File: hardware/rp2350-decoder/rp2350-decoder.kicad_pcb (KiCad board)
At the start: 6 copper layers, 19.9 x 8.8 mm, 67 parts, among them J1 SWDIO, J2 SWCLK, J3 5052702412, Q1 DMN2991UDA-7B, Q2 DMN2991UDA-7B, Q3 NST847BPDP6T5G, Q4 NST847BPDP6T5G, Q5 DMN2991UDA-7B, Q6 DMN2991UDA-7B, Q7 DMN2991UDA-7B, Q8 DMN2991UDA-7B, SW1 BOOT, U1 NCS2220AMUT1G, U2 AP63203WU, U3 W25Q128JVPIQ, U4 RP2350A, U5 MAX98357AEWL+T, U6 MD9927, Y1 X252012MMB4SI

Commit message: chore: pcb cleanup
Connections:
- net /GPIO21 renamed /DCC_TTL
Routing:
- net GND: track 7.85 -> 6.09 mm
- net +3.3V: track 30.9 -> 29.6 mm
- net /CAP_VDC: track 11.8 -> 10.9 mm
- net /QSPI_CS: track 11.1 -> 10.4 mm

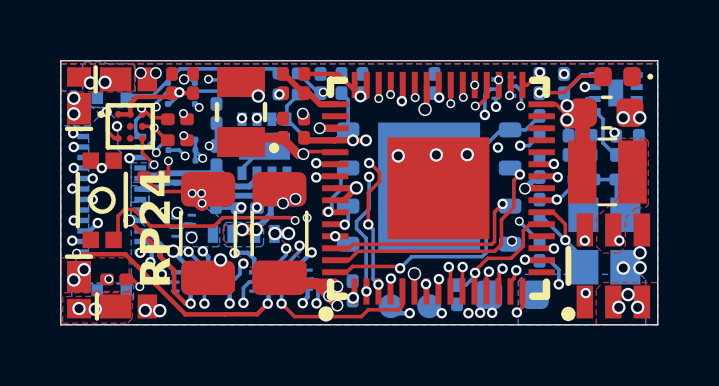
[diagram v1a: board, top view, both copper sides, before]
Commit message: chore: rearrange i2s pins for easier pio use
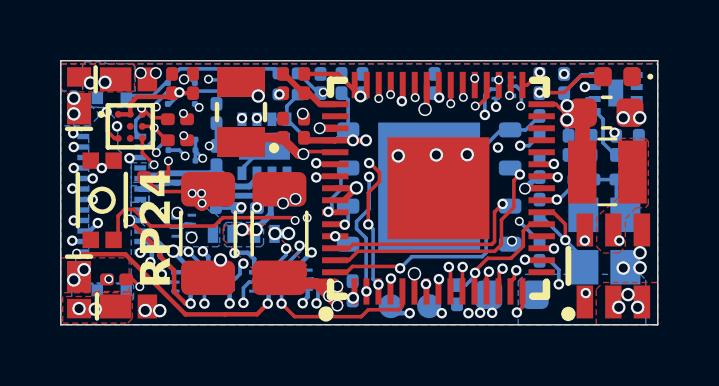
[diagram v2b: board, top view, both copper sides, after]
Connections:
- U4 pad 34: /I2S_LRCLK -> /I2S_DIN
- U4 pad 35: /I2S_DIN -> /I2S_BCLK
- U4 pad 36: /I2S_BCLK -> /I2S_LRCLK
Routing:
- net /I2S_LRCLK: track 17.8 -> 15.8 mm
- net /I2S_BCLK: track 16.0 -> 14.1 mm
- net /I2S_DIN: track 13.1 -> 14.5 mm
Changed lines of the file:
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@@
 			(size 0.88 0.2)
 			(layers "F.Cu" "F.Paste" "F.Mask")
-			(net 39 "/I2S_LRCLK")
+			(net 37 "/I2S_DIN")
 			(pinfunction "GPIO22")
 			(pintype "unspecified")
@@
 			(size 0.88 0.2)
 			(layers "F.Cu" "F.Paste" "F.Mask")
-			(net 37 "/I2S_DIN")
+			(net 38 "/I2S_BCLK")
 			(pinfunction "GPIO23")
 			(pintype "unspecified")
@@
 			(size 0.88 0.2)
 			(layers "F.Cu" "F.Paste" "F.Mask")
-			(net 38 "/I2S_BCLK")
+			(net 39 "/I2S_LRCLK")
 			(pinfunction "GPIO24")
 			(pintype "unspecified")
@@
 		(net 33)
 	)
+	(segment
+		(start 114.2 100.97)
+		(end 114.2 100.56)
+		(width 0.12)
+		(layer "F.Cu")
+		(net 37)
+	)
+	(segment
+		(start 113.817602 101.260002)
+		(end 113.909998 101.260002)
+		(width 0.12)
+		(layer "F.Cu")
+		(net 37)
+	)
+	(segment
+		(start 113.909998 101.260002)
+		(end 114.2 100.97)
+		(width 0.12)
+		(layer "F.Cu")
+		(net 37)
+	)
 	(via
 		(at 101.87707 101.935026)
@@
 	)
 	(via
-		(at 113.8 100.56)
+		(at 113.817602 101.260002)
 		(size 0.3)
 		(drill 0.2)
@@
 	)
 	(segment
-		(start 104.440769 100.946004)
-		(end 104.238673 101.1481)
+		(start 104.796542 100.946004)
+		(end 105.492546 100.25)
 		(width 0.12)
 		(layer "In4.Cu")
@@
 	)
 	(segment
-		(start 101.87707 101.637546)
-		(end 101.87707 101.935026)
+		(start 104.238673 101.1481)
+		(end 104.440769 100.946004)
 		(width 0.12)
 		(layer "In4.Cu")
@@
 	)
 	(segment
-		(start 103.340573 100.97)
-		(end 102.544616 100.97)
+		(start 104.440769 100.946004)
+		(end 104.796542 100.946004)
 		(width 0.12)
 		(layer "In4.Cu")
@@
 	)
 	(segment
-		(start 113.49 100.25)
-		(end 105.492546 100.25)
+		(start 105.492546 100.25)
+		(end 113.2 100.25)
 		(width 0.12)
 		(layer "In4.Cu")
@@
 	)
 	(segment
-		(start 105.492546 100.25)
-		(end 104.796542 100.946004)
+		(start 103.340573 100.97)
+		(end 103.518673 101.1481)
 		(width 0.12)
 		(layer "In4.Cu")
@@
 	)
 	(segment
-		(start 113.8 100.56)
-		(end 113.49 100.25)
+		(start 101.87707 101.935026)
+		(end 101.87707 101.637546)
 		(width 0.12)
 		(layer "In4.Cu")
@@
 	)
 	(segment
-		(start 103.518673 101.1481)
-		(end 103.340573 100.97)
+		(start 113.2 100.25)
+		(end 113.817602 100.867602)
 		(width 0.12)
 		(layer "In4.Cu")
@@
 	)
 	(segment
-		(start 104.238673 101.1481)
-		(end 103.518673 101.1481)
+		(start 101.87707 101.637546)
+		(end 102.544616 100.97)
 		(width 0.12)
 		(layer "In4.Cu")
@@
 	)
 	(segment
-		(start 104.796542 100.946004)
-		(end 104.440769 100.946004)
+		(start 113.817602 100.867602)
+		(end 113.817602 101.260002)
 		(width 0.12)
 		(layer "In4.Cu")
@@
 	)
 	(segment
-		(start 102.544616 100.97)
-		(end 101.87707 101.637546)
+		(start 103.518673 101.1481)
+		(end 104.238673 101.1481)
 		(width 0.12)
 		(layer "In4.Cu")
@@
 	)
 	(segment
-		(start 101.53207 102.07793)
-		(end 101.79134 102.3372)
+		(start 102.544616 100.97)
+		(end 103.340573 100.97)
 		(width 0.12)
-		(layer "F.Cu")
-		(net 38)
+		(layer "In4.Cu")
+		(net 37)
 	)
 	(segment
-		(start 113.4 100.95)
-		(end 113.4 100.56)
+		(start 101.53207 102.07793)
+		(end 101.79134 102.3372)
 		(width 0.12)
 		(layer "F.Cu")
@@
 		(net 38)
 	)
-	(segment
-		(start 113.42 100.97)
-		(end 113.4 100.95)
-		(width 0.12)
-		(layer "F.Cu")
-		(net 38)
-	)
 	(via
-		(at 113.42 100.97)
+		(at 113.8 100.34)
 		(size 0.3)
 		(drill 0.2)
@@
 	)
 	(segment
-		(start 103.3319 100.660196)
-		(end 102.322059 100.660196)
-		(width 0.12)
-		(layer "In4.Cu")
-		(net 38)
-	)
-	(segment
-		(start 113.937904 100.91)
-		(end 114.145 100.702904)
-		(width 0.12)
-		(layer "In4.Cu")
-		(net 38)
-	)
-	(segment
-		(start 114.145 100.412904)
-		(end 113.752096 100.02)
-		(width 0.12)
-		(layer "In4.Cu")
-		(net 38)
-	)
-	(segment
-		(start 113.752096 100.02)
-		(end 103.972096 100.02)
+		(start 102.322059 100.660196)
+		(end 101.527275 101.45498)
 		(width 0.12)
 		(layer "In4.Cu")
@@
 	)
 	(segment
-		(start 113.42 100.97)
-		(end 113.48 100.91)
+		(start 103.3319 100.660196)
+		(end 102.322059 100.660196)
 		(width 0.12)
 		(layer "In4.Cu")
@@
 	)
 	(segment
-		(start 102.322059 100.660196)
-		(end 101.527275 101.45498)
+		(start 113.48 100.02)
+		(end 103.972096 100.02)
 		(width 0.12)
 		(layer "In4.Cu")
@@
 	)
 	(segment
-		(start 113.48 100.91)
-		(end 113.937904 100.91)
+		(start 113.8 100.34)
+		(end 113.48 100.02)
 		(width 0.12)
 		(layer "In4.Cu")
@@
 	)
 	(segment
-		(start 114.145 100.702904)
-		(end 114.145 100.412904)
+		(start 113.4 100.95)
+		(end 113.4 100.56)
 		(width 0.12)
-		(layer "In4.Cu")
-		(net 38)
+		(layer "F.Cu")
+		(net 39)
 	)
 	(segment
@@
 	)
 	(segment
-		(start 114.2 100.97)
-		(end 114.2 100.56)
-		(width 0.12)
-		(layer "F.Cu")
-		(net 39)
-	)
-	(segment
-		(start 113.817602 101.260002)
-		(end 113.909998 101.260002)
-		(width 0.12)
-		(layer "F.Cu")
-		(net 39)
-	)
-	(segment
-		(start 113.909998 101.260002)
-		(end 114.2 100.97)
+		(start 113.42 100.97)
+		(end 113.4 100.95)
 		(width 0.12)
 		(layer "F.Cu")
@@
 	)
 	(via
-		(at 113.817602 101.260002)
+		(at 113.42 100.97)
 		(size 0.3)
 		(drill 0.2)
@@
 	)
 	(segment
-		(start 113.817602 101.260002)
-		(end 114.16 100.917604)
+		(start 102.333733 101.180883)
+		(end 102.333733 102.43769)
 		(width 0.12)
 		(layer "In3.Cu")
@@
 	)
 	(segment
-		(start 114.16 100.432096)
-		(end 113.747904 100.02)
+		(start 102.333733 102.43769)
+		(end 103.112033 103.21599)
 		(width 0.12)
 		(layer "In3.Cu")
@@
 	)
 	(segment
-		(start 102.333733 101.180883)
-		(end 102.333733 102.43769)
+		(start 111.79 100.02)
+		(end 103.83326 100.02)
 		(width 0.12)
 		(layer "In3.Cu")
@@
 	)
 	(segment
-		(start 102.333733 102.43769)
-		(end 103.112033 103.21599)
+		(start 112.47 100.02)
+		(end 113.42 100.97)
 		(width 0.12)
 		(layer "In3.Cu")
@@
 	)
 	(segment
-		(start 114.16 100.917604)
-		(end 114.16 100.432096)
+		(start 111.79 100.02)
+		(end 112.47 100.02)
 		(width 0.12)
 		(layer "In3.Cu")
@@
 		(width 0.12)
 		(layer "In3.Cu")
-		(net 39)
-	)
-	(segment
-		(start 113.747904 100.02)
-		(end 103.83326 100.02)
-		(width 0.12)
-		(layer "In3.Cu")
